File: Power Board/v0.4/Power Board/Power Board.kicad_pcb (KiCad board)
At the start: 2 copper layers, 66 x 80 mm, 72 parts, among them J1 Battery In, J2 JST B2PS-VH, J3 JST B2PS-VH, J4 JST B2PS-VH, J5 JST B2PS-VH, J6 JST B2PS-VH, J7 JST B2PS-VH, J8 Molex 70553-0006, Q1 SI5504BDC, SW1 SW_Push, U1 LMZ14203, U2 TPS53819A, U3 CSD86360Q5D

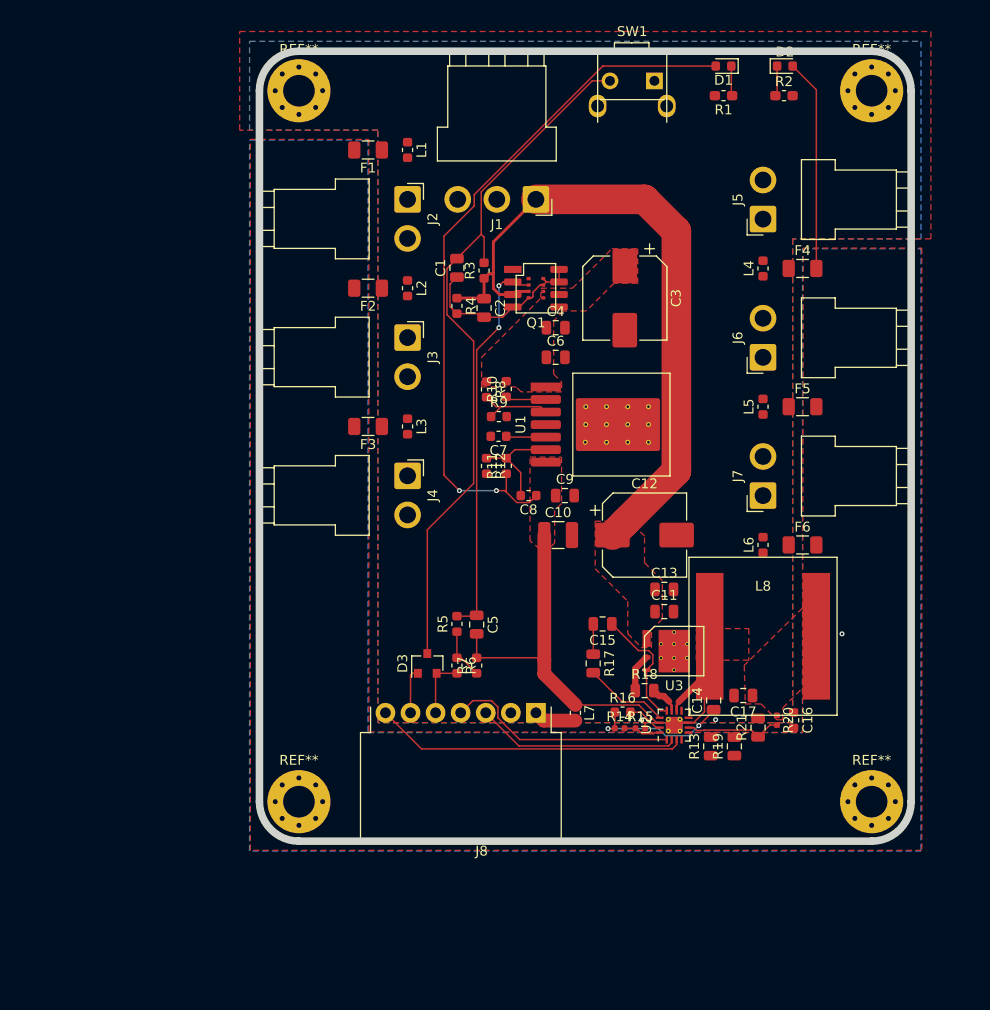
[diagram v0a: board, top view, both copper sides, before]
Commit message: New 4 Layer Layout
Needed 4 layers and double sided design in order to make everything fit
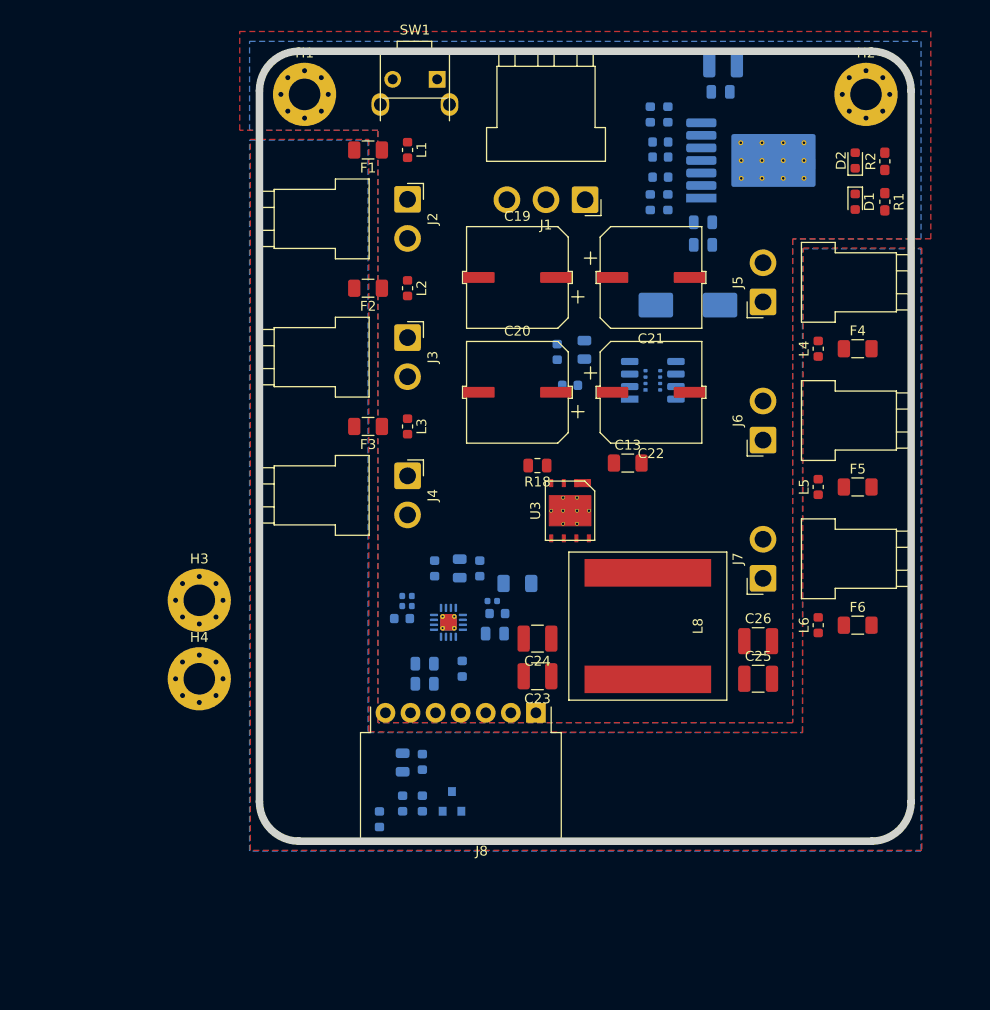
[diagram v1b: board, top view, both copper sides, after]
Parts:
- removed C12: 100µF, Capacitor_SMD:CP_Elec_8x10
- removed REF** (x4): MountingHole_3.2mm_M3_Pad_Via, MountingHole:MountingHole_3.2mm_M3_Pad_Via
- added C19: 47µF, Power_Board:CP_OSCON_Poly_F12, F.Cu at (103.1, 57.9)
- added C20: 47µF, Power_Board:CP_OSCON_Poly_F12, F.Cu at (103.1, 69.5)
- added C21: 47µF, Power_Board:CP_OSCON_Poly_F12, F.Cu at (116.7, 57.9)
- added C22: 47µF, Power_Board:CP_OSCON_Poly_F12, F.Cu at (116.7, 69.5)
- added C23: 47µF, Capacitor_SMD:C_1210_3225Metric, F.Cu at (105.2, 98.3)
- added C24: 47µF, Capacitor_SMD:C_1210_3225Metric, F.Cu at (105.2, 94.5)
- added C25: 47µF, Capacitor_SMD:C_1210_3225Metric, F.Cu at (127.5, 98.6)
- added C26: 47µF, Capacitor_SMD:C_1210_3225Metric, F.Cu at (127.5, 94.7)
- added H1: M3, MountingHole:MountingHole_3.2mm_M3_Pad_Via, F.Cu at (81.6, 39.4)
- added H2: M3, MountingHole:MountingHole_3.2mm_M3_Pad_Via, F.Cu at (138.4, 39.4)
- added H3: M3, MountingHole:MountingHole_3.2mm_M3_Pad_Via, F.Cu at (70.9, 90.6)
- added H4: M3, MountingHole:MountingHole_3.2mm_M3_Pad_Via, F.Cu at (70.9, 98.6)
- C1, C10, C11, C15, C16, C2, C3, C4, C5, C6, C7, C8, C9, D3, L7, Q1, R10, R11, R12, R14, R15, R16, R17, R19, R20, R3, R4, R5, R6, R7, R8, R9, U1, U2: moved to B.Cu
- C13: footprint Capacitor_SMD:C_0805_2012Metric -> Capacitor_SMD:C_1206_3216Metric
- C14: footprint Capacitor_SMD:C_0805_2012Metric -> Capacitor_SMD:C_0603_1608Metric; moved to B.Cu
- C17: footprint Capacitor_SMD:C_0805_2012Metric -> Capacitor_SMD:C_1206_3216Metric; moved to B.Cu
- R13, R21: footprint Resistor_SMD:R_0805_2012Metric -> Resistor_SMD:R_0603_1608Metric; moved to B.Cu
- moved C10 50.5 mm to (124.0, 36.3)
- moved C9 43.8 mm to (123.7, 39.1)
- moved C8 41.1 mm to (118.4, 41.4), turned to 270 degrees
- moved R11 38.5 mm to (116.6, 41.4), turned to 270 degrees
- moved R12 37.2 mm to (117.6, 44.2), turned to 180 degrees
- moved C1 36.4 mm to (131.9, 46.5), turned to 180 degrees
- moved C16 35.3 mm to (99.3, 87.4), turned to 90 degrees
- moved R13 33.3 mm to (94.7, 87.4)
- moved R19 33.1 mm to (97.3, 87.4)
- moved C7 32.7 mm to (117.6, 45.7)
- moved R20 31.2 mm to (100.6, 90.7), turned to 0 degrees
- moved R9 29.2 mm to (117.6, 47.8), turned to 180 degrees
- moved R21 28.8 mm to (101.1, 91.9), turned to 0 degrees
- moved R15 27.2 mm to (91.9, 90.2), turned to 180 degrees
- moved C14 25.7 mm to (97.5, 97.5), turned to 270 degrees
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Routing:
- net /5.2V_switched: track 109.3 -> 0.00 mm, vias 2 -> 0
- net /Pi Power/Power_Button: track 72.0 -> 0.00 mm
- net /Battery_Power: track 69.8 -> 0.00 mm
- net Net-(C5-Pad1): track 39.6 -> 0.00 mm, vias 2 -> 0
- net /Panel_Alert: track 31.7 -> 0.00 mm
- net /SCL: track 23.7 -> 0.00 mm
- net /Panel_Power: track 21.5 -> 0.00 mm, vias 1 -> 0
- net /SDA: track 20.7 -> 0.00 mm
- net Net-(C1-Pad1): track 18.2 -> 0.00 mm
- net /Panel Power/Vreg: track 14.5 -> 0.00 mm, vias 2 -> 0
- net Net-(C15-Pad1): track 12.6 -> 0.00 mm
- net Net-(C8-Pad2): track 10.8 -> 0.00 mm
- net Net-(R20-Pad2): track 9.85 -> 0.00 mm
- net Net-(R17-Pad2): track 8.63 -> 0.00 mm
- net Net-(R8-Pad2): track 8.04 -> 0.00 mm
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- removed copper zone on F.Cu, net /5.2V_switched
- removed copper zone on F.Cu, net /Battery_Power
- removed copper zone on F.Cu, net /Panel Power/Switch_Node
- removed copper zone on F.Cu, net /Pi Power/Vin_switched

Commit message: Preliminary Layout Started
Have most of the components moved to reasonable locations.
Initial layout placeholders to get a general sense of connections.
Added a sheet with the MPU-9250 Circuit but not pushed to board yet.
Still need to add a lot of copper pours and stitching.
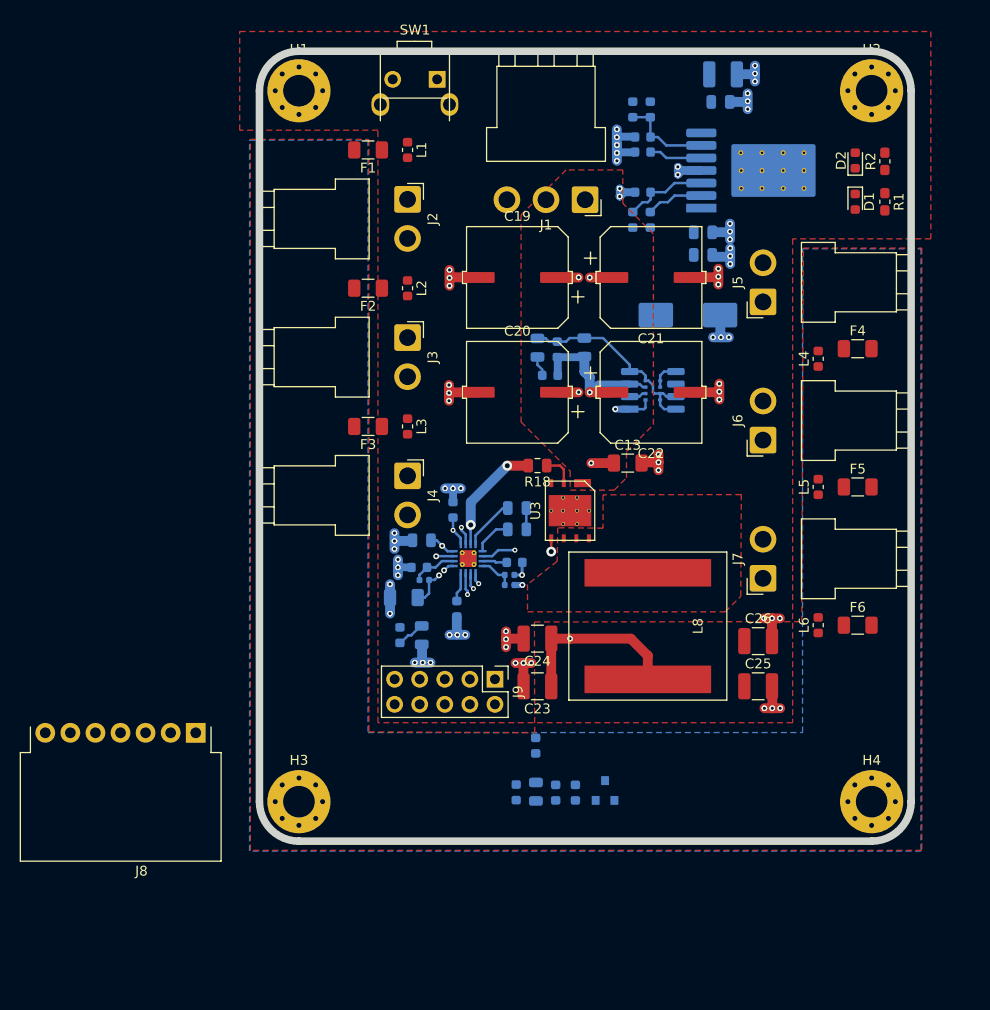
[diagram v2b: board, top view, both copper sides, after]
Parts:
- added J9: Conn_02x05_Odd_Even, Connector_PinHeader_2.54mm:PinHeader_2x05_P2.54mm_Vertical, F.Cu at (100.8, 98.6)
- moved H4 69.2 mm to (139.0, 111.0)
- moved J8 34.5 mm to (70.5, 104.0)
- moved C1 32.5 mm to (105.2, 65.0), turned to 270 degrees
- moved H3 22.8 mm to (81.0, 111.0)
- moved C15 20.1 mm to (103.1, 81.3), turned to 0 degrees
- moved L7 17.5 mm to (105.0, 105.3), turned to 90 degrees
- moved R17 16.5 mm to (103.1, 83.4)
- moved C14 16.1 mm to (96.6, 81.4), turned to 90 degrees
- moved D3 15.5 mm to (112.0, 109.9)
- moved R6 15.5 mm to (109.0, 110.1)
- moved R7 15.5 mm to (107.0, 110.1)
- moved C5 13.8 mm to (105.0, 110.0), turned to 90 degrees
- moved R16 12.7 mm to (102.8, 86.8), turned to 180 degrees
- moved C11 12.0 mm to (93.4, 84.5), turned to 180 degrees
- moved C17 11.6 mm to (91.6, 90.3), turned to 180 degrees
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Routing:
- net GND: track 0.00 -> 91.5 mm, vias 0 -> 71
- net /Battery_Power: track 0.00 -> 48.6 mm, vias 0 -> 6
- net /Panel_Power: track 0.00 -> 41.2 mm, vias 0 -> 3
- net Net-(C1-Pad1): track 0.00 -> 21.8 mm
- net /Panel Power/Vreg: track 0.00 -> 16.7 mm, vias 0 -> 2
- net /Panel Power/Drive_Low: track 0.00 -> 14.0 mm, vias 0 -> 2
- net /Panel Power/Drive_High_1: track 0.00 -> 11.6 mm, vias 0 -> 2
- net Net-(C8-Pad2): track 0.00 -> 9.28 mm
- net Net-(R8-Pad2): track 0.00 -> 8.59 mm
- net Net-(R10-Pad1): track 0.00 -> 5.85 mm
- net Net-(C7-Pad1): track 0.00 -> 5.38 mm
- net Net-(C15-Pad1): track 0.00 -> 5.30 mm
- net Net-(R20-Pad2): track 0.00 -> 4.57 mm
- net Net-(R17-Pad2): track 0.00 -> 3.96 mm
- net Net-(R14-Pad2): track 0.00 -> 3.63 mm
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- added copper zone on F.Cu, net /Battery_Power
- added copper zone on F.Cu, net /Panel Power/Switch_Node
- added copper zone on In1.Cu, net GND
- removed copper zone on B.Cu, net GND
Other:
- copper layers 2 -> 4
- net class Default: via_dia 0.508 -> 0.6; via_drill 0.254 -> 0.3
- net class Panel_Drive: via_dia 0.508 -> 1; via_drill 0.254 -> 0.5
- net class Pi_Battery: via_dia 1.016 -> 1; via_drill 0.508 -> 0.5
- net class Pi_Power: via_dia 0.508 -> 1; via_drill 0.254 -> 0.5

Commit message: Updated board dimensions and mt. holes, tweaked MPU schematic.
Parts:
- removed H1, H2, H3, H4: M3, MountingHole:MountingHole_3.2mm_M3_Pad_Via
- added C27: 100nF, Capacitor_SMD:C_0603_1608Metric, F.Cu at (87.0, 127.0)
- added C28: 100nF, Capacitor_SMD:C_0603_1608Metric, F.Cu at (87.0, 129.5)
- added C29: 10nF, Capacitor_SMD:C_0603_1608Metric, F.Cu at (91.0, 127.0)
- added REF**: MountingHole_2.7mm_M2.5, MountingHole:MountingHole_2.7mm_M2.5, F.Cu at (80.5, 38.5)
- added REF**: MountingHole_2.7mm_M2.5, MountingHole:MountingHole_2.7mm_M2.5, F.Cu at (80.5, 111.5)
- added REF**: MountingHole_2.7mm_M2.5, MountingHole:MountingHole_2.7mm_M2.5, F.Cu at (143.5, 111.5)
- added REF**: MountingHole_2.7mm_M2.5, MountingHole:MountingHole_2.7mm_M2.5, F.Cu at (143.5, 38.5)
- added U4: MPU-9250, Sensor_Motion:InvenSense_QFN-24_3x3mm_P0.4mm, F.Cu at (82.4, 128.3)
- J9: footprint Connector_PinHeader_2.54mm:PinHeader_2x05_P2.54mm_Vertical -> Connector_JST:JST_PUD_S10B-PUDSS-1_2x05_P2.00mm_Horizontal
- moved J9 13.1 mm to (89.5, 92.0)
- moved J5 4.02 mm to (132.0, 60.0)
- moved J6 4.02 mm to (132.0, 74.0)
- moved J7 4.00 mm to (132.0, 88.4)
- moved L4 1.96 mm to (132.0, 65.0)
- moved F4 1.69 mm to (135.9, 65.0)
- moved F5 1.59 mm to (136.0, 79.0)
- moved F6 1.59 mm to (136.0, 93.1)
- moved L5 1.59 mm to (132.0, 79.1)
- moved L6 1.59 mm to (132.0, 93.1)
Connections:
- J8 pad 3: /SDA -> SDA
- J8 pad 4: /SCL -> SCL
- J9 pad 1: Net-(J9-Pad1) -> Pi_3.3V
- J9 pad 10: Net-(J9-Pad10) -> /Power_Sense
- J9 pad 2: Net-(J9-Pad2) -> /+5.2V
- J9 pad 3: Net-(J9-Pad3) -> SDA
- J9 pad 4: Net-(J9-Pad4) -> /+5.2V
- J9 pad 5: Net-(J9-Pad5) -> SCL
- J9 pad 6: Net-(J9-Pad6) -> GND
- J9 pad 7: Net-(J9-Pad7) -> /Panel_Alert
- J9 pad 8: Net-(J9-Pad8) -> /Power_Ctl
- J9 pad 9: Net-(J9-Pad9) -> GND
- U2 pad 1: /SCL -> SCL
- U2 pad 2: /SDA -> SDA
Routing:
- net SDA: track 0.00 -> 1.70 mm, vias 0 -> 1
- net /SDA: track 1.70 -> 0.00 mm, vias 1 -> 0
- net SCL: track 0.00 -> 1.21 mm, vias 0 -> 1
- net /SCL: track 1.21 -> 0.00 mm, vias 1 -> 0
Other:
- board size 66 x 80 mm -> 70 x 80 mm
- board text added: "No components over 4mm tall in this region"

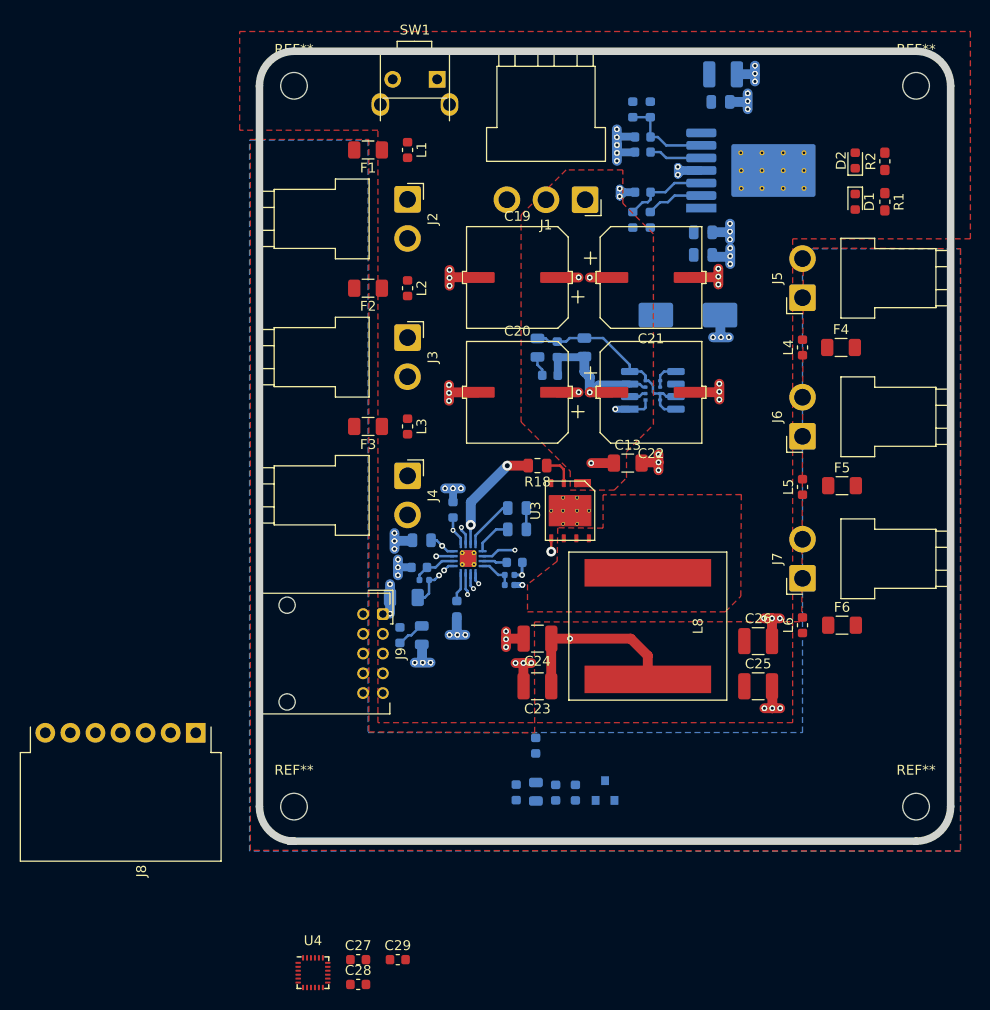
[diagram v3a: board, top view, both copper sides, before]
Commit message: Revert "Updated board dimensions and mt. holes, tweaked MPU schematic."
This reverts commit 6936a160ef8a0f8efd2e8f2d18775030a6ae8800.
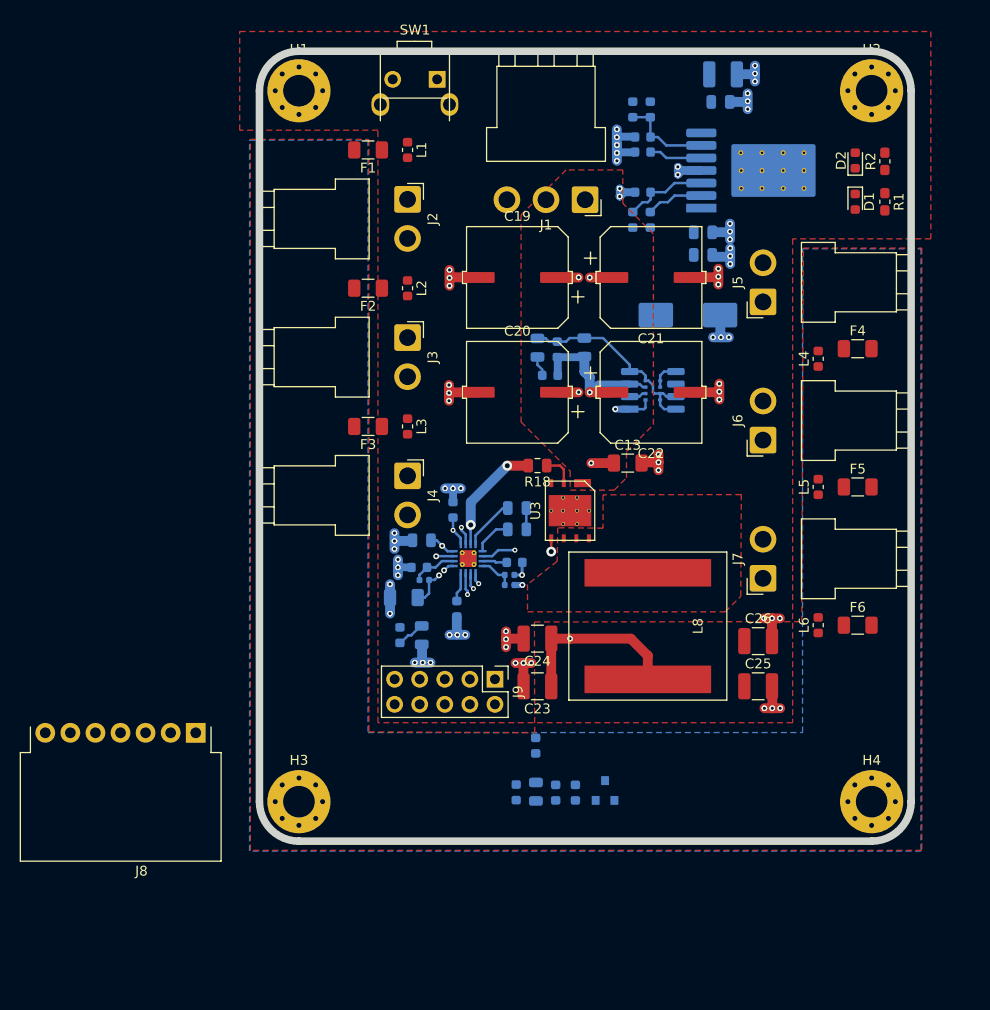
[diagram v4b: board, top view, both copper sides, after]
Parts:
- removed C27, C28: 100nF, Capacitor_SMD:C_0603_1608Metric
- removed C29: 10nF, Capacitor_SMD:C_0603_1608Metric
- removed REF** (x4): MountingHole_2.7mm_M2.5, MountingHole:MountingHole_2.7mm_M2.5
- removed U4: MPU-9250, Sensor_Motion:InvenSense_QFN-24_3x3mm_P0.4mm
- added H1: M3, MountingHole:MountingHole_3.2mm_M3_Pad_Via, F.Cu at (81.0, 39.0)
- added H2: M3, MountingHole:MountingHole_3.2mm_M3_Pad_Via, F.Cu at (139.0, 39.0)
- added H3: M3, MountingHole:MountingHole_3.2mm_M3_Pad_Via, F.Cu at (81.0, 111.0)
- added H4: M3, MountingHole:MountingHole_3.2mm_M3_Pad_Via, F.Cu at (139.0, 111.0)
- J9: footprint Connector_JST:JST_PUD_S10B-PUDSS-1_2x05_P2.00mm_Horizontal -> Connector_PinHeader_2.54mm:PinHeader_2x05_P2.54mm_Vertical
- moved J9 13.1 mm to (100.8, 98.6)
- moved J5 4.02 mm to (128.0, 60.4)
- moved J6 4.02 mm to (128.0, 74.4)
- moved J7 4.00 mm to (128.0, 88.4)
- moved L4 1.96 mm to (133.6, 66.1)
- moved F4 1.69 mm to (137.6, 65.1)
- moved F5 1.59 mm to (137.6, 79.1)
- moved F6 1.59 mm to (137.6, 93.1)
- moved L5 1.59 mm to (133.6, 79.1)
- moved L6 1.59 mm to (133.6, 93.1)
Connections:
- J8 pad 3: SDA -> /SDA
- J8 pad 4: SCL -> /SCL
- J9 pad 1: Pi_3.3V -> Net-(J9-Pad1)
- J9 pad 10: /Power_Sense -> Net-(J9-Pad10)
- J9 pad 2: /+5.2V -> Net-(J9-Pad2)
- J9 pad 3: SDA -> Net-(J9-Pad3)
- J9 pad 4: /+5.2V -> Net-(J9-Pad4)
- J9 pad 5: SCL -> Net-(J9-Pad5)
- J9 pad 6: GND -> Net-(J9-Pad6)
- J9 pad 7: /Panel_Alert -> Net-(J9-Pad7)
- J9 pad 8: /Power_Ctl -> Net-(J9-Pad8)
- J9 pad 9: GND -> Net-(J9-Pad9)
- U2 pad 1: SCL -> /SCL
- U2 pad 2: SDA -> /SDA
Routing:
- net SDA: track 1.70 -> 0.00 mm, vias 1 -> 0
- net /SDA: track 0.00 -> 1.70 mm, vias 0 -> 1
- net SCL: track 1.21 -> 0.00 mm, vias 1 -> 0
- net /SCL: track 0.00 -> 1.21 mm, vias 0 -> 1
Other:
- board size 70 x 80 mm -> 66 x 80 mm
- board text removed: "No components over 4mm tall in this region"

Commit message: More Layout Work
Just another preliminary update so we can both work on changes
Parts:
- moved D2 4.74 mm to (137.2, 50.8), turned to 270 degrees
- moved R2 4.66 mm to (140.0, 50.8)
- moved R1 4.29 mm to (140.0, 46.0), turned to 90 degrees
- moved D1 4.27 mm to (137.2, 46.0), turned to 90 degrees
- moved R14 0.76 mm to (102.3, 88.8)
- moved R16 0.76 mm to (102.8, 87.5)
- moved R15 0.76 mm to (102.3, 89.8)
- moved R3 0.25 mm to (106.4, 68.1)
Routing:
- net /5.2V_switched: track 3.53 -> 37.2 mm, vias 1 -> 2
- net /Pi Power/Vin_switched: track 2.94 -> 33.2 mm
- net /Panel Power/Switch_Node: track 0.00 -> 23.9 mm, vias 0 -> 2
- net Net-(C15-Pad1): track 5.30 -> 11.5 mm, vias 0 -> 1
- net Net-(D2-Pad1): track 0.00 -> 3.93 mm
- net Net-(C5-Pad1): track 1.73 -> 4.84 mm, vias 0 -> 1
- net Net-(D1-Pad1): track 0.00 -> 2.83 mm
- net GND: track 91.5 -> 93.8 mm, vias 71 -> 73
- net Net-(R14-Pad2): track 3.63 -> 4.69 mm
- net /Pi Power/Power_Button: track 2.06 -> 2.89 mm, vias 0 -> 1
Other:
- net class /Panel_Power	Pi_Powerr added: clearance 0.5, trace_width 0.254, via_dia 0.6, via_drill 0.3
- net class Default: trace_width 0.1524 -> 0.254
- net class Pi_Battery: clearance 0.1524 -> 0.3
- net class Pi_Power: clearance 0.1524 -> 0.3
- rule via_min_size: 0.508 -> 0.3
